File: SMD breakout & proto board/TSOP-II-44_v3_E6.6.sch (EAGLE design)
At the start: 7 parts

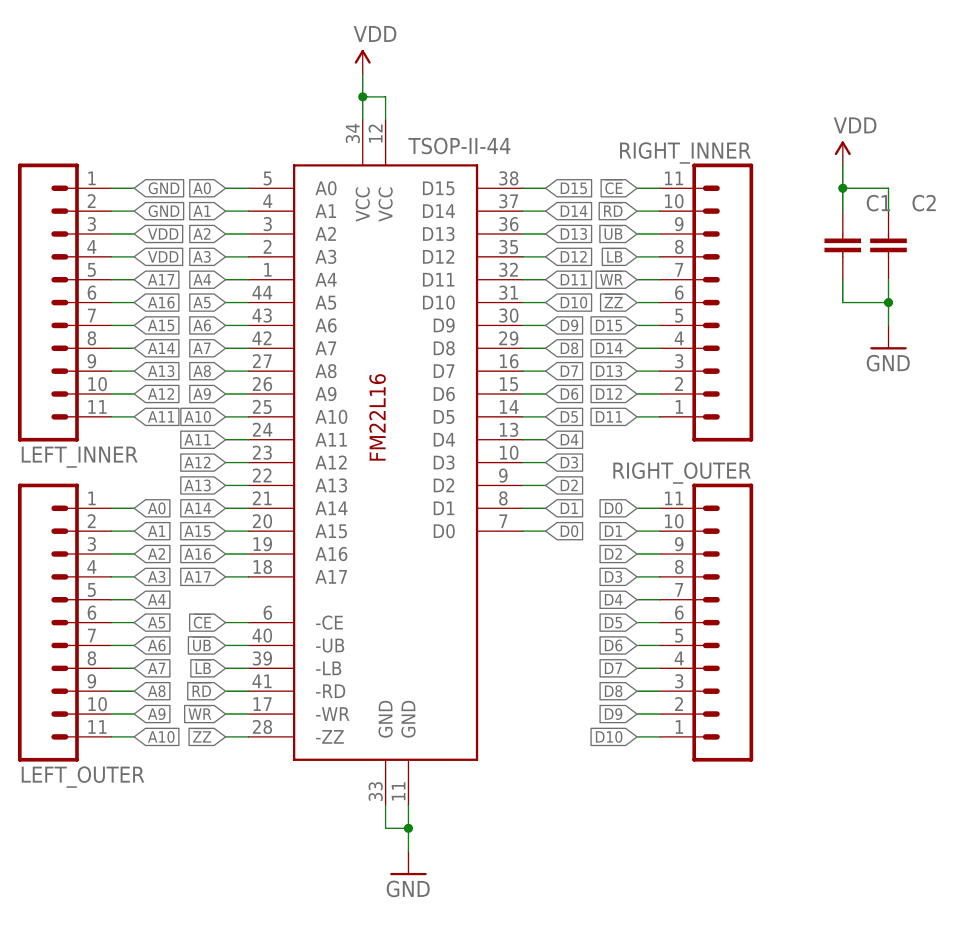
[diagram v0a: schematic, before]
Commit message: swapped supply pins
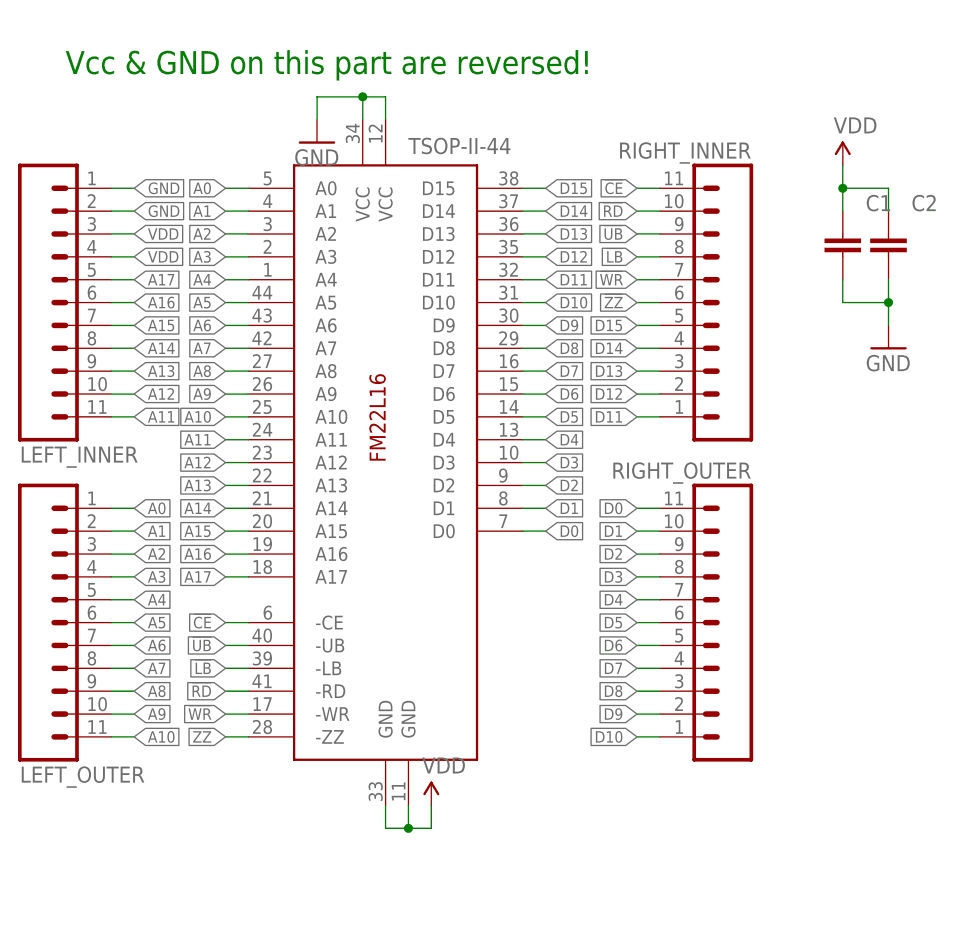
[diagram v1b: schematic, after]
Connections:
- net GND: now also TSOP-II-44.VCC@1, TSOP-II-44.VCC@2; no longer TSOP-II-44.GND@1, TSOP-II-44.GND@2
- net VDD: now also TSOP-II-44.GND@1, TSOP-II-44.GND@2; no longer TSOP-II-44.VCC@1, TSOP-II-44.VCC@2
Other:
- note added: "Vcc & GND on this part are reversed!"
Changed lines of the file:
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@@
 <sheet>
 <plain>
+<text x="7.62" y="88.9" size="2.54" layer="91">Vcc &amp; GND on this part are reversed!</text>
 </plain>
 <instances>
@@
 <instance part="C1" gate="C" x="93.98" y="68.58"/>
 <instance part="C2" gate="C" x="99.06" y="68.58"/>
-<instance part="GND1" gate="1" x="45.72" y="0"/>
-<instance part="SUPPLY1" gate="VDD" x="40.64" y="88.9"/>
+<instance part="GND1" gate="1" x="35.56" y="81.28"/>
+<instance part="SUPPLY1" gate="VDD" x="48.26" y="7.62"/>
 <instance part="SUPPLY2" gate="VDD" x="93.98" y="78.74"/>
 <instance part="GND2" gate="1" x="99.06" y="58.42"/>
@@
 <nets>
 <net name="GND" class="0">
-<segment>
-<pinref part="TSOP-II-44" gate="G$1" pin="GND@2"/>
-<wire x1="43.18" y1="7.62" x2="43.18" y2="5.08" width="0.1524" layer="91"/>
-<pinref part="TSOP-II-44" gate="G$1" pin="GND@1"/>
-<wire x1="45.72" y1="7.62" x2="45.72" y2="5.08" width="0.1524" layer="91"/>
-<wire x1="43.18" y1="5.08" x2="45.72" y2="5.08" width="0.1524" layer="91"/>
-<wire x1="45.72" y1="5.08" x2="45.72" y2="2.54" width="0.1524" layer="91"/>
-<pinref part="GND1" gate="1" pin="GND"/>
-<junction x="45.72" y="5.08"/>
-</segment>
 <segment>
 <pinref part="C1" gate="C" pin="2"/>
@@
 <label x="15.24" y="76.2" size="1.27" layer="95" xref="yes"/>
 </segment>
-</net>
-<net name="VDD" class="0">
 <segment>
+<pinref part="GND1" gate="1" pin="GND"/>
+<wire x1="35.56" y1="83.82" x2="35.56" y2="86.36" width="0.1524" layer="91"/>
 <pinref part="TSOP-II-44" gate="G$1" pin="VCC@1"/>
 <wire x1="43.18" y1="86.36" x2="43.18" y2="83.82" width="0.1524" layer="91"/>
@@
 <wire x1="40.64" y1="83.82" x2="40.64" y2="86.36" width="0.1524" layer="91"/>
 <wire x1="43.18" y1="86.36" x2="40.64" y2="86.36" width="0.1524" layer="91"/>
-<wire x1="40.64" y1="86.36" x2="40.64" y2="88.9" width="0.1524" layer="91"/>
-<pinref part="SUPPLY1" gate="VDD" pin="VDD"/>
+<wire x1="35.56" y1="86.36" x2="40.64" y2="86.36" width="0.1524" layer="91"/>
 <junction x="40.64" y="86.36"/>
 </segment>
+</net>
+<net name="VDD" class="0">
 <segment>
 <pinref part="C1" gate="C" pin="1"/>
@@
 <label x="15.24" y="71.12" size="1.27" layer="95" xref="yes"/>
 </segment>
+<segment>
+<pinref part="SUPPLY1" gate="VDD" pin="VDD"/>
+<wire x1="48.26" y1="7.62" x2="48.26" y2="5.08" width="0.1524" layer="91"/>
+<pinref part="TSOP-II-44" gate="G$1" pin="GND@2"/>
+<wire x1="43.18" y1="7.62" x2="43.18" y2="5.08" width="0.1524" layer="91"/>
+<pinref part="TSOP-II-44" gate="G$1" pin="GND@1"/>
+<wire x1="45.72" y1="7.62" x2="45.72" y2="5.08" width="0.1524" layer="91"/>
+<wire x1="43.18" y1="5.08" x2="45.72" y2="5.08" width="0.1524" layer="91"/>
+<wire x1="48.26" y1="5.08" x2="45.72" y2="5.08" width="0.1524" layer="91"/>
+<junction x="45.72" y="5.08"/>
+</segment>
 </net>
